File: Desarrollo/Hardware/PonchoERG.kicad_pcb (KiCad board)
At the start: 2 copper layers, 86.4 x 96.5 mm, 85 parts, among them J1 Entradas Analógicas, J2 I/O's Multi Propósito, U1 TPD2E001, U10 ADS1299, U11 ADuM6401, U12 ADuM2401, U13 NCP1117ST33T3G, U14 OPA2376_NI, U2 TPD2E001, U3 TPD2E001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

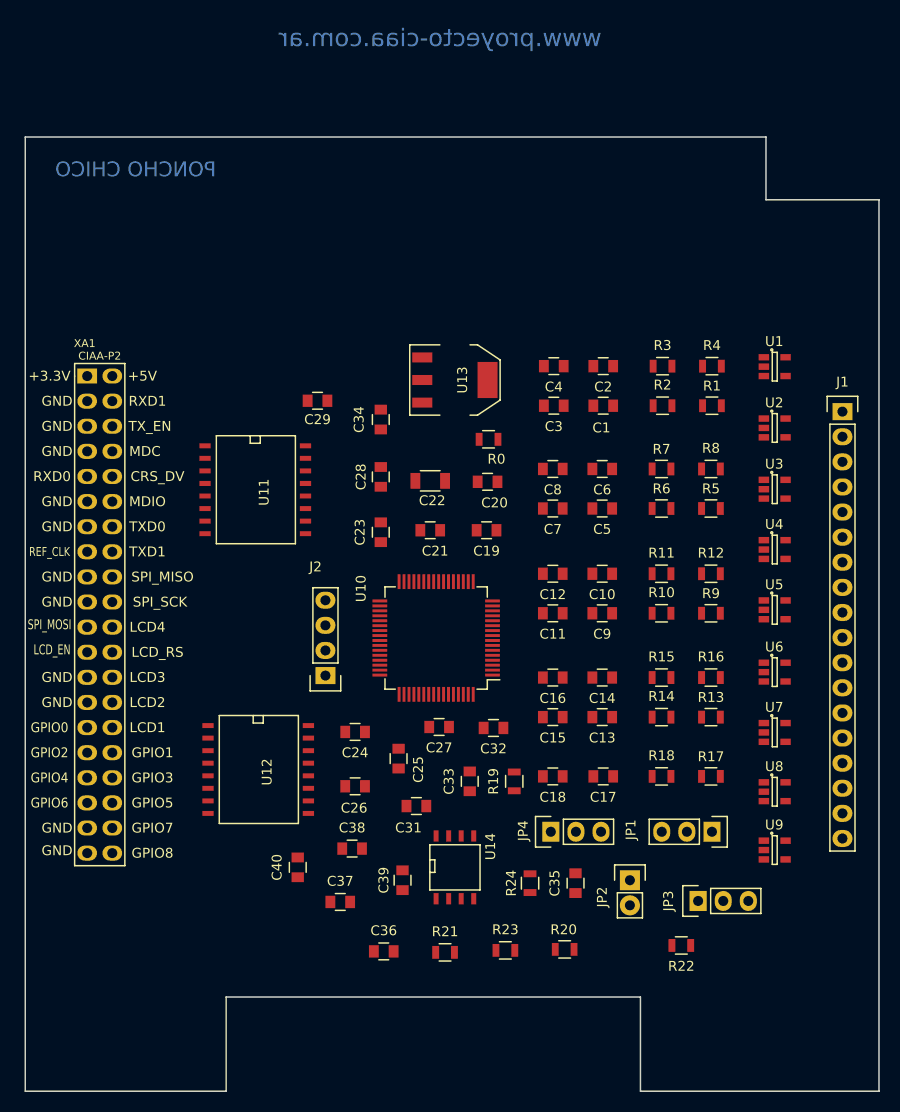
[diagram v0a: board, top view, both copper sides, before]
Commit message: Finalización de primer ruteo estimado. Revisión de cantidad de v
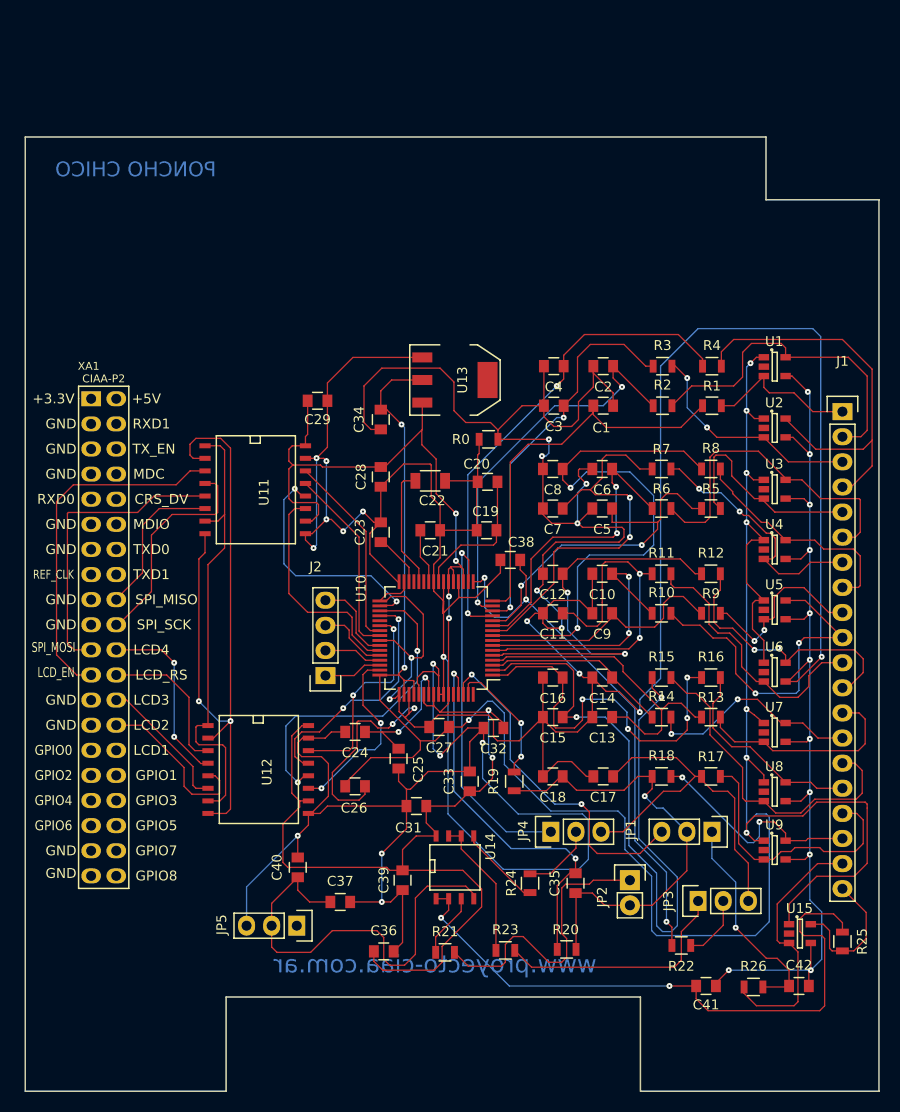
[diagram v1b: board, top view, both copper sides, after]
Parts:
- added C41: 1nF, Capacitors_SMD:C_0805, F.Cu at (170.0, 129.3)
- added C42: 1nF, Capacitors_SMD:C_0805, F.Cu at (179.4, 129.3)
- added JP5: -AVSS, Pin_Headers:Pin_Header_Straight_1x03, F.Cu at (128.6, 123.2)
- added R25: 2.2k, Resistors_SMD:R_0805, F.Cu at (183.8, 124.8)
- added R26: 2.2k, Resistors_SMD:R_0805, F.Cu at (174.8, 129.4)
- added U15: TPD2E001, TO_SOT_Packages_SMD:SOT-23-5, F.Cu at (179.5, 124.0)
- J1: footprint Pin_Headers:Pin_Header_Straight_1x18 -> Pin_Headers:Pin_Header_Straight_1x20
- moved C38 33.3 mm to (150.2, 86.2)
- moved XA1 2.33 mm to (107.8, 69.9)
- moved R20 0.20 mm to (155.9, 125.6)
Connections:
- C37 pad 1: GNDA -> Net-(C37-Pad1)
- C40 pad 1: GNDA -> Net-(C37-Pad1)
- JP1 pad 1: (no net) -> /ADS1299/BIAS_ELEC
- U14 pad 4: GNDA -> Net-(C37-Pad1)
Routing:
- net Earth: track 0.00 -> 418.3 mm, vias 0 -> 25
- net GNDA: track 0.00 -> 280.4 mm, vias 0 -> 13
- net +3V3: track 0.00 -> 240.2 mm, vias 0 -> 10
- net +5V: track 0.00 -> 161.7 mm, vias 0 -> 6
- net /ADS1299/IN8+: track 0.00 -> 72.1 mm, vias 0 -> 2
- net /AISLACIÓN/GND_NISO: track 0.00 -> 71.7 mm, vias 0 -> 2
- net /ADS1299/BIAS_SHD: track 0.00 -> 63.9 mm, vias 0 -> 2
- net /ADS1299/IN4-: track 0.00 -> 56.6 mm, vias 0 -> 2
- net Net-(C38-Pad2): track 0.00 -> 55.0 mm, vias 0 -> 3
- net /ADS1299/IN2-: track 0.00 -> 49.4 mm, vias 0 -> 2
- net /ADS1299/BIAS_DRV: track 0.00 -> 46.8 mm, vias 0 -> 1
- net /AISLACIÓN/+5V_NISO: track 0.00 -> 46.7 mm
- net Net-(C37-Pad1): track 0.00 -> 45.0 mm
- net Net-(J1-Pad4): track 0.00 -> 42.6 mm
- net /ADS1299/IN6-: track 0.00 -> 41.5 mm, vias 0 -> 2
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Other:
- net class Default: clearance 0.508 -> 0.1; trace_width 0.381 -> 0.1; via_drill 0.4 -> 0.2
- rule trace_clearance: 0.508 -> 0.1
- rule trace_min: 0.2 -> 0.1
- rule via_min_drill: 0.3 -> 0.2
- rule via_min_size: 0.4 -> 0.6

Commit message: Añadidura de zonas de aislación y separación de ZONA ISO y NO_ISO. Zonas de relleno de cobre finalizada. Ninguna (ni top ni bottom) se encuentran unidas a alguna red (ni de masa ni nada similar). Esto sujeto a revisión próxima reunión.
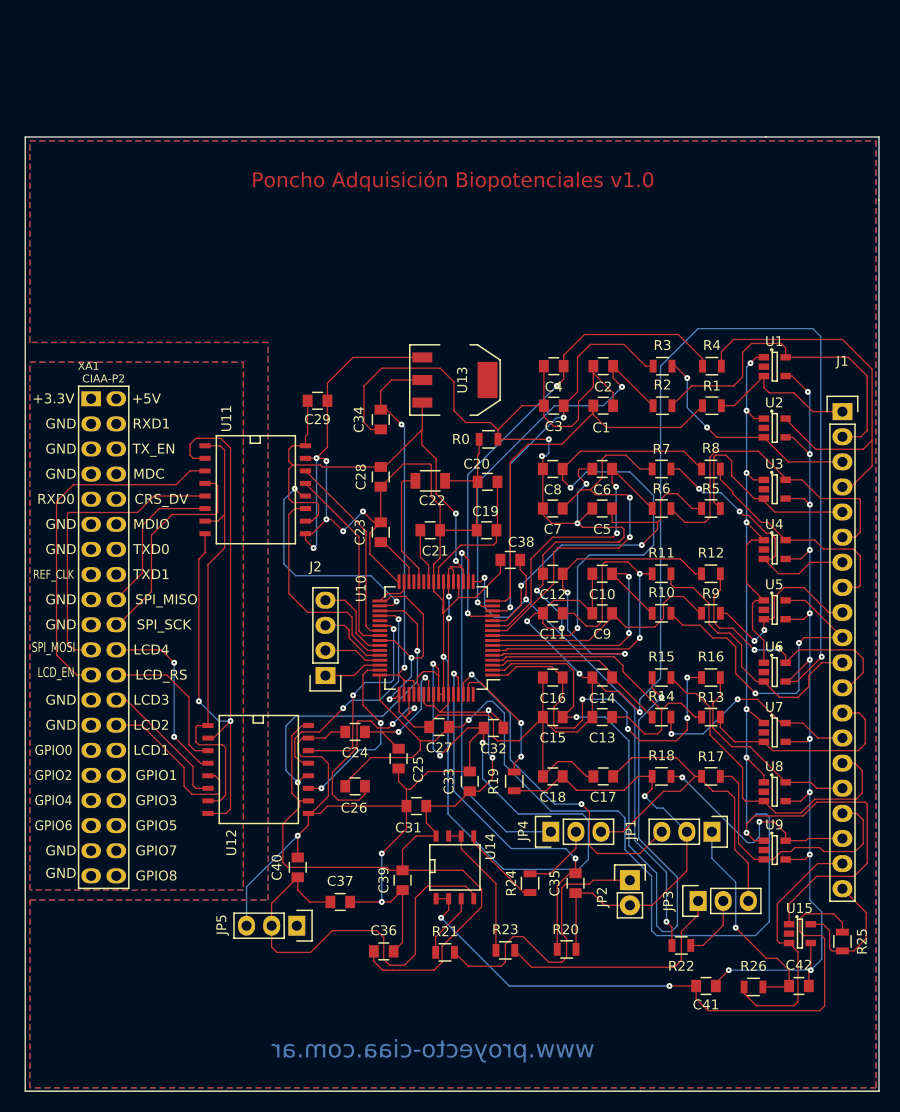
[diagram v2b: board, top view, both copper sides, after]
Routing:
- added copper zone on B.Cu, net (none)
- added copper zone on F.Cu, net (none)
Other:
- outline, holes or cut-outs redrawn
- board text added: "Poncho Adquisición Biopotenciales v1.0"
- board text removed: "PONCHO CHICO"
